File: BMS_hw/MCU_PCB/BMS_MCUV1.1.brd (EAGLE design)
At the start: 60 x 30 mm, 48 parts, among them IC2 SST25VF020B804ISA, Q1 CRYSTALS-GND-LID-IQXC-42

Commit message: pdf , brd and sch itt@26
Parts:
- removed TP1, TP2, TP5: TP-SMD60, simpa:TP-SMD60
- moved C11 45.7 mm to (8.26, 4.83)
- moved R4 44.6 mm to (6.99, 6.99)
- moved C10 41.5 mm to (7.54, 9.53), turned to 180 degrees
- moved R3 40.4 mm to (9.53, 6.99)
- moved R7 38.5 mm to (8.26, 8.26)
- moved C9 36.7 mm to (10.2, 9.53), turned to 0 degrees
- moved C17 35.4 mm to (43.0, 18.9)
- moved C8 33.7 mm to (14.0, 10.2)
- moved U$1 29.2 mm to (8.89, 17.1), turned to 270 degrees
- moved L2 28.6 mm to (41.3, 6.35), turned to 0 degrees
- moved C22 27.5 mm to (50.2, 15.9), turned to 270 degrees
- moved L3 26.0 mm to (47.0, 15.2), turned to 0 degrees
- moved L4 24.4 mm to (50.2, 12.1), turned to 90 degrees
- moved R6 23.9 mm to (8.26, 24.8), turned to 270 degrees
- moved C18 21.4 mm to (44.4, 12.8), turned to 180 degrees
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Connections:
- net N$11 renamed R4/R3/C11
- net N$32 renamed AVDD
- removed net N$4: C19.1, MCU2.10
- removed net N$9: C18.1, MCU2.26
- removed net VDD38: C17.1, MCU2.38
- net !MCLR: no longer TP5.P$1
- net 3.3V: now also IC2.7
- net GND: now also JP2.8; no longer IC2.7, JP2.6, JP2.9
- net PGEC2: now also JP2.11; no longer JP2.10, TP2.P$1
- net PGED2: now also JP2.10; no longer JP2.11, TP1.P$1
- net RX_1: now also JP2.7; no longer JP2.8
- net RX_2: now also JP2.6; no longer JP2.5
- net S-LED_1: now also MCU2.54; no longer MCU2.49
- net S-LED_2: now also MCU2.53; no longer MCU2.50
- net S-LED_3: now also MCU2.52; no longer MCU2.51
- net S-LED_4: now also MCU2.51; no longer MCU2.52
- net S-LED_5: now also MCU2.50; no longer MCU2.53
- net S-LED_6: now also MCU2.49; no longer MCU2.54
- net TX_1: now also JP2.5; no longer JP2.7
- net VDD: now also C17.1, C18.1, C19.1, JP2.9, MCU2.10, MCU2.26, MCU2.38
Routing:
- net 3.3V: track 116.6 -> 40.8 mm, vias 5 -> 2
- net CANH: track 6.91 -> 47.3 mm, vias 0 -> 1
- net CAN_TX: track 10.4 -> 42.4 mm, vias 0 -> 2
- net R4/R3/C11: track 35.1 -> 5.97 mm, vias 3 -> 0
- net CAN_RX: track 12.8 -> 39.2 mm, vias 0 -> 2
- net PGEC2: track 48.7 -> 22.5 mm
- net KEY-IN: track 43.5 -> 20.4 mm, vias 3 -> 1
- net TX_2: track 51.5 -> 29.0 mm, vias 3 -> 1
- net RDD: track 35.5 -> 13.2 mm, vias 2 -> 1
- net VDD: track 9.96 -> 31.9 mm, vias 0 -> 15
- net PGED2: track 43.7 -> 22.3 mm
- net RX_1: track 57.4 -> 36.8 mm
- net CANL: track 28.1 -> 48.7 mm
- net 5V: track 29.5 -> 49.3 mm, vias 0 -> 1
- net FLOUT: track 26.5 -> 6.81 mm
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- added copper zone on layer 1, net VDD
- added copper zone on layer 15, net VDD
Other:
- board text added: "!MCLR"
- board text added: "3.3V"
- board text added: "GND"
- board text added: "PGEC2"
- board text added: "PGED2"
- board text added: "RX_1"
- board text added: "RX_2"
- board text added: "TX_1"
- board text added: "TX_2"
- board text added: "VDD"
- board text added: "VSS"

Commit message: updated
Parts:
- moved C19 3.42 mm to (24.1, 9.53), turned to 180 degrees
- moved C20 2.08 mm to (38.5, 7.62), turned to 0 degrees
- moved C17 1.27 mm to (43.0, 17.6)
- moved Q1 0.90 mm to (41.9, 21.6)
- moved C13 0.64 mm to (34.3, 24.1)
- moved JP1 0.64 mm to (31.8, 3.81)
- moved JP5 0.63 mm to (31.8, 26.7)
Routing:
- net !MCLR: track 52.5 -> 50.7 mm, vias 2 -> 3
- net GND: track 10.1 -> 8.78 mm, vias 14 -> 15
- net AVDD: track 6.23 -> 7.46 mm
- net VDD: track 31.9 -> 33.1 mm
- net 3.3V: track 40.8 -> 39.9 mm
- net KEY-IN: track 20.4 -> 19.8 mm
- net CANH: track 47.3 -> 47.9 mm
- net SCLK: track 15.0 -> 14.4 mm
- net S-LED_2: track 14.7 -> 14.1 mm
- net S-LED_6: track 7.63 -> 6.99 mm
- net S-LED_3: track 13.0 -> 12.3 mm
- net S-LED_1: track 16.1 -> 15.4 mm
- net MOSI: track 16.7 -> 16.1 mm
- net CHG_GATE: track 23.9 -> 23.2 mm
- net S-LED_5: track 8.67 -> 8.08 mm
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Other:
- board text added: "Greenfuel Energy Solutions Pvt. Ltd"
- board text added: "MCUV1.1"

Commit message: fdghfn
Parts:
- moved C11 0.64 mm to (7.62, 4.83)
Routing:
- net 3.3V: track 39.9 -> 0.00 mm, vias 2 -> 0
- net RX_1: track 36.8 -> 0.00 mm, vias 1 -> 0
- net TX_1: track 36.6 -> 0.00 mm, vias 1 -> 0
- net RX_2: track 35.4 -> 0.00 mm, vias 1 -> 0
- net !MCLR: track 50.7 -> 17.7 mm, vias 3 -> 0
- net TX_2: track 29.0 -> 0.00 mm, vias 1 -> 0
- net VDD: track 33.1 -> 11.0 mm, vias 15 -> 0
- net PGEC2: track 22.0 -> 0.00 mm
- net PGED2: track 21.7 -> 0.00 mm
- net KEY-IN: track 19.8 -> 0.00 mm, vias 1 -> 0
- net 5V: track 49.8 -> 31.6 mm, vias 1 -> 0
- net MOSI: track 16.1 -> 0.00 mm
- net S-LED_1: track 15.4 -> 0.00 mm
- net OLED_SCL: track 15.2 -> 0.00 mm
- net CSB: track 15.1 -> 0.00 mm
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
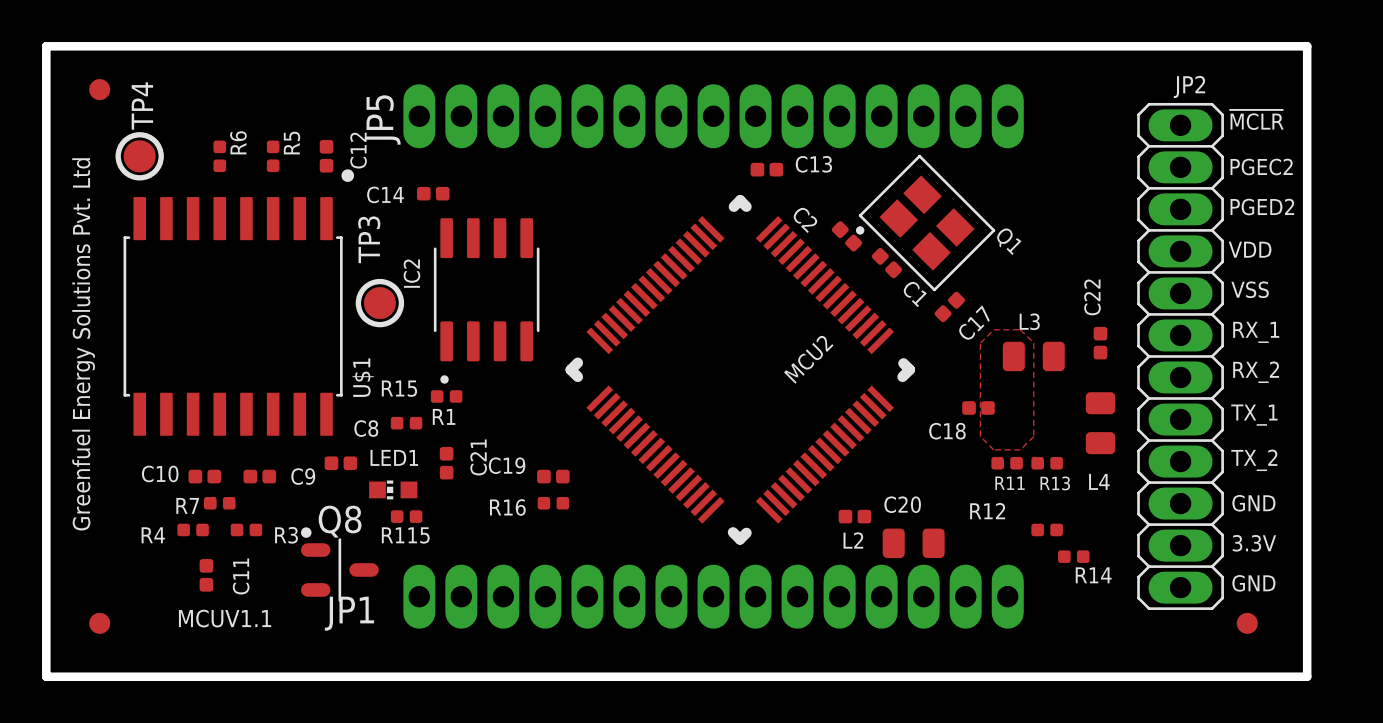
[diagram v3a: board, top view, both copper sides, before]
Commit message: piggy top layer routed 50%
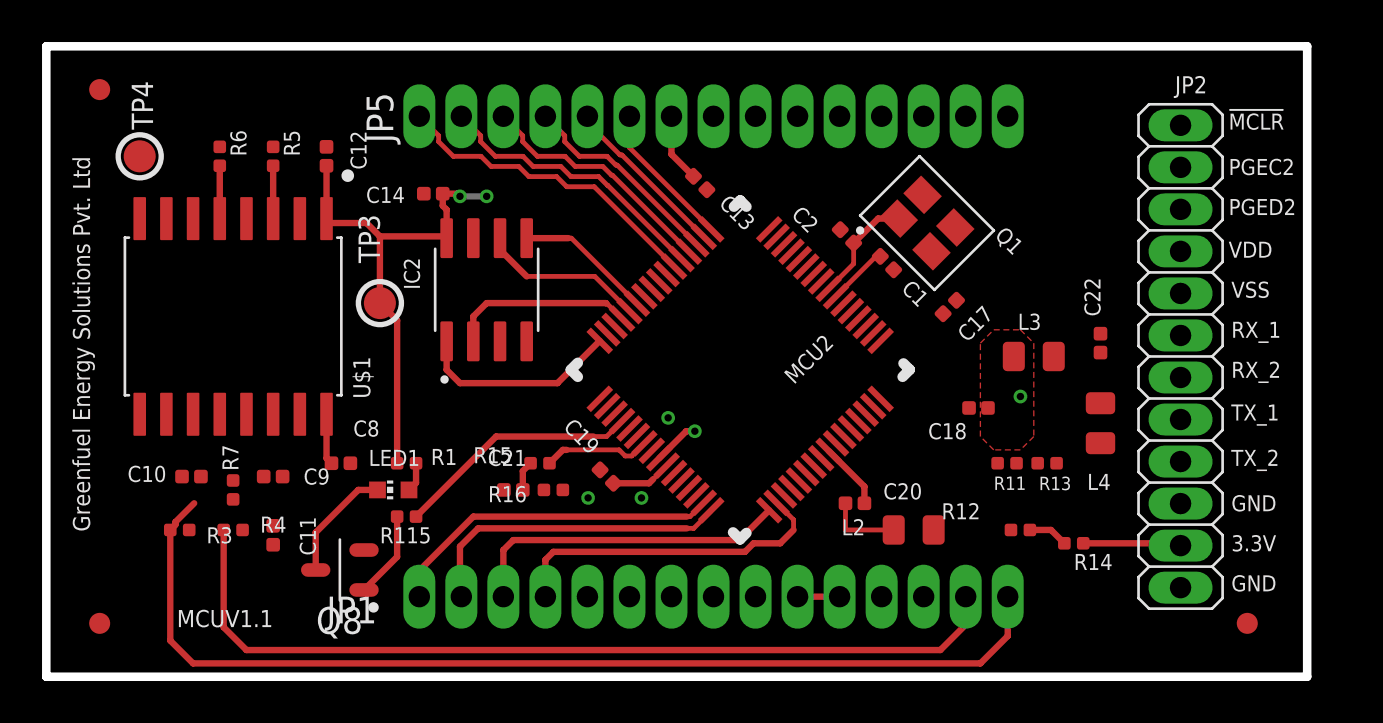
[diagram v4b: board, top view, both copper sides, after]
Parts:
- moved R15 5.46 mm to (23.5, 10.2)
- moved C11 3.70 mm to (10.8, 6.73)
- moved C21 3.42 mm to (22.2, 8.89), turned to 180 degrees
- moved C13 3.24 mm to (31.1, 23.5), turned to 315 degrees
- moved R3 3.18 mm to (6.35, 6.99)
- moved C19 2.54 mm to (26.7, 9.53), turned to 135 degrees
- moved R4 1.91 mm to (8.89, 6.99), turned to 0 degrees
- moved R1 1.90 mm to (17.1, 10.2)
- moved R12 1.27 mm to (46.4, 6.99)
- moved R7 0.90 mm to (8.89, 8.89), turned to 270 degrees
- moved C20 0.64 mm to (38.5, 8.26)
- moved L2 0.64 mm to (41.3, 6.99)
- moved C10 0.63 mm to (6.91, 9.53)
- moved C9 0.63 mm to (10.8, 9.53)
- moved R14 0.63 mm to (48.9, 6.35)
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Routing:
- net CAN_TX: track 39.0 -> 0.00 mm
- net CAN_RX: track 35.7 -> 0.00 mm
- net 3.3V: track 0.00 -> 32.1 mm, vias 0 -> 3
- net 5V: track 31.6 -> 4.43 mm
- net !OLED_SDA: track 24.6 -> 0.00 mm
- net !OLED_SCL: track 21.1 -> 0.00 mm
- net PCHG_GATE: track 20.4 -> 0.00 mm
- net CHG_GATE: track 20.4 -> 0.00 mm
- net DSG_GATE: track 18.2 -> 0.00 mm
- net MOSI: track 0.00 -> 16.1 mm
- net CSB: track 0.00 -> 15.8 mm
- net MISO: track 0.00 -> 15.7 mm
- net S-LED_1: track 0.00 -> 15.3 mm
- net SCLK: track 0.00 -> 15.1 mm
- net S-LED_2: track 0.00 -> 13.5 mm
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
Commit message: fhyffj
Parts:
- moved R7 1.27 mm to (8.89, 10.2), turned to 0 degrees
- moved C10 0.63 mm to (6.91, 8.89)
- moved C9 0.63 mm to (10.8, 8.89)
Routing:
- net PCHG_GATE: track 0.00 -> 25.1 mm, vias 0 -> 1
- net CHG_GATE: track 0.00 -> 20.4 mm, vias 0 -> 1
- net CANH: track 49.7 -> 69.1 mm
- net KEY-IN: track 0.00 -> 17.6 mm, vias 0 -> 1
- net DSG_GATE: track 0.00 -> 16.9 mm
- net CANL: track 42.2 -> 48.7 mm
- net R4/R3/C11: track 0.00 -> 1.54 mm

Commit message: fryfjhf
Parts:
- moved C17 2.98 mm to (45.9, 18.2), turned to 90 degrees
- moved C1 1.80 mm to (41.3, 18.4)
- moved C2 1.42 mm to (39.4, 20.3)
- moved Q1 0.90 mm to (42.5, 21.0)
- turned C19 to 180 degrees
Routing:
- net !MCLR: track 5.15 -> 45.3 mm, vias 0 -> 1
- net PGED2: track 0.00 -> 20.4 mm
- net PGEC2: track 0.00 -> 20.3 mm
- net DSG_GATE: track 16.9 -> 22.2 mm, vias 0 -> 2
- net N$1: track 2.89 -> 7.85 mm
- net GND: track 5.43 -> 1.20 mm
- net N$2: track 5.30 -> 2.00 mm
- net KEY-IN: track 17.6 -> 20.1 mm
- net 5V: track 4.43 -> 2.43 mm
